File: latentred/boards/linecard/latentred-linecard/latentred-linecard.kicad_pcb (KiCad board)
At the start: 4 copper layers, 168 x 92 mm, 438 parts, among them J1 CONN_LATENTRED_LINECARD_DEVICE, J2 STEWART_SS_74500_024, Q1 SSM6N58NU, Q2 SSM6N58NU, Q3 SSM6N58NU, Q4 SSM6N58NU, Q5 SSM6N58NU, Q6 SSM6N58NU, Q7 SSM6N58NU, Q8 SSM6N58NU, U1 MCP1703T-3302E, U10 DP83867, U11 DP83867, U12 DP83867, U13 DP83867, U14 DP83867, U15 DP83867, U16 DSC6101CI2A-025.0000, U17 5PB1108CMG, U2 LTC3374-QFN, U3 SI7050, U4 LTC2451, U5 INA226, U6 INA226, U7 INA226, U8 DP83867, U9 DP83867

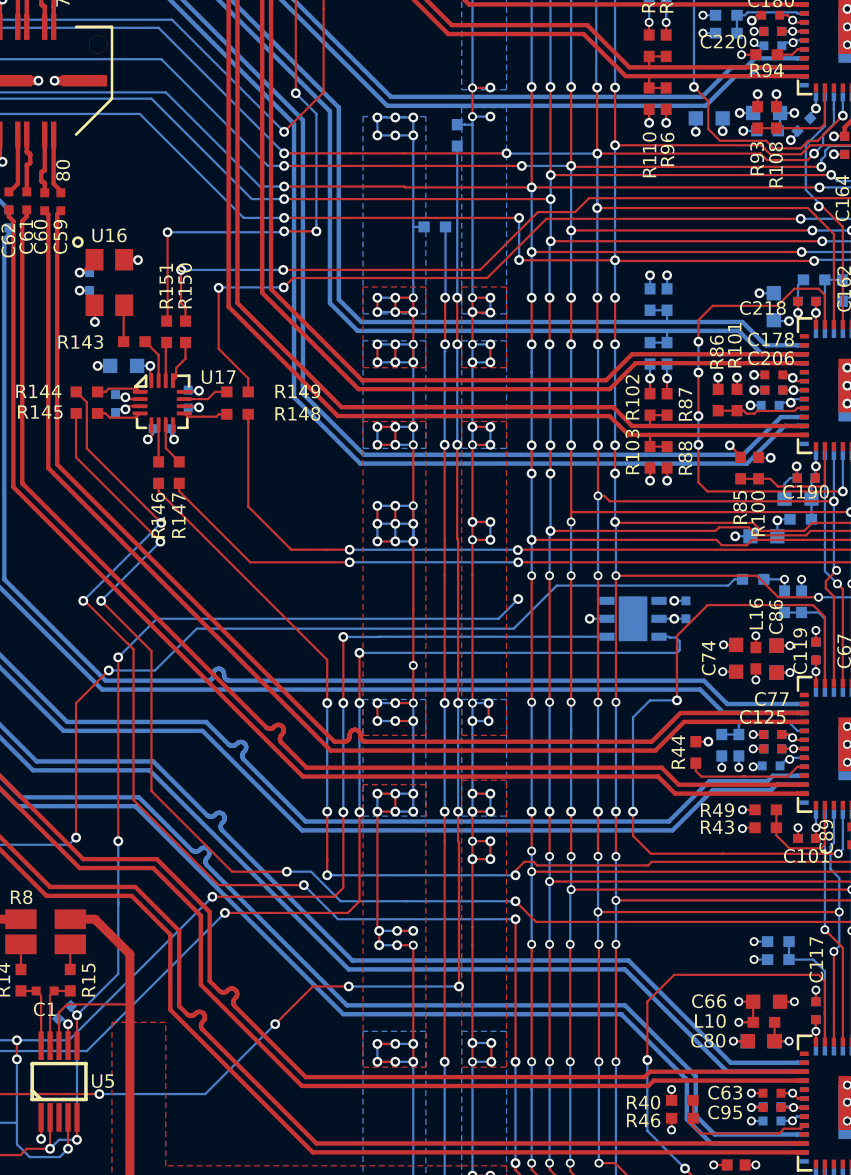
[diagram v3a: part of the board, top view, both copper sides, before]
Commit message: Continued routing line card PCB
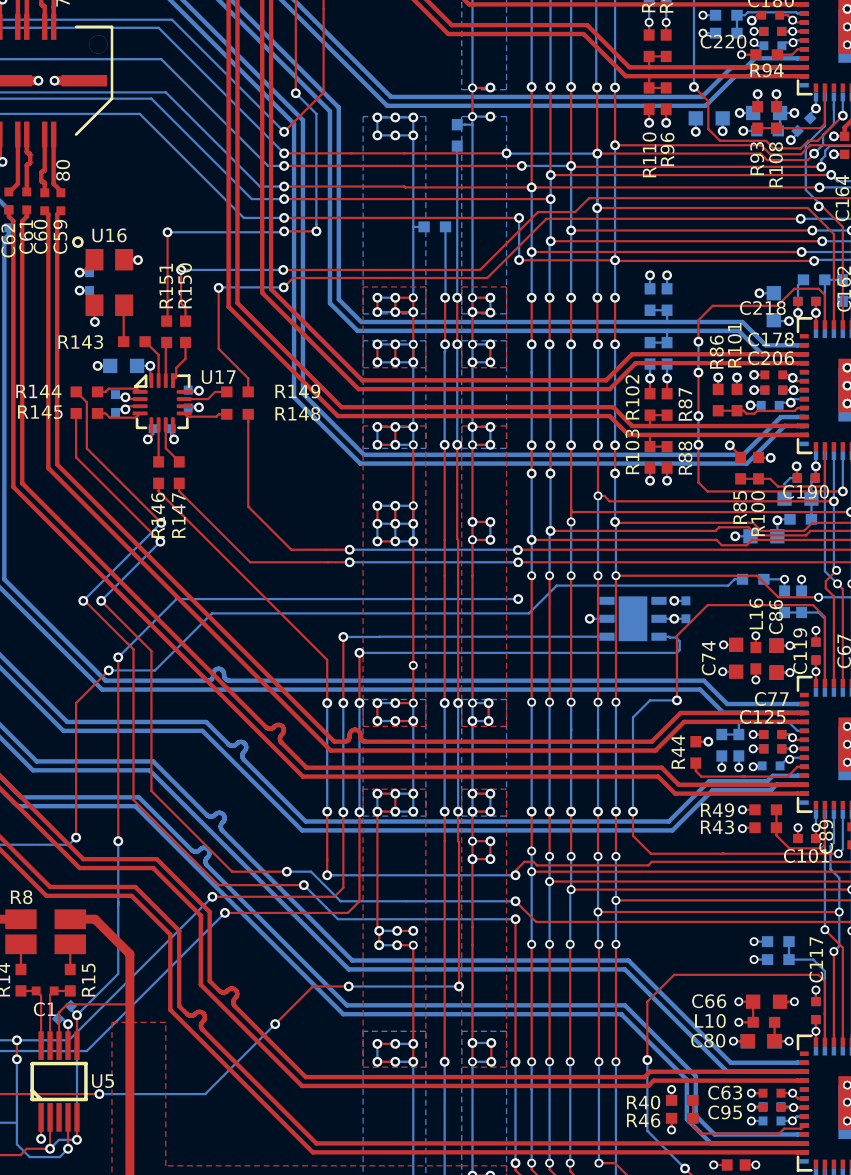
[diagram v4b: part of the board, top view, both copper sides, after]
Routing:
- net /PHYs/1V8: track 513.7 -> 516.6 mm
- net /PHYs/A2V5_1: track 14.6 -> 15.4 mm
- net /PHYs/A2V5_3: track 15.9 -> 16.5 mm
- added copper zone on In2.Cu, net /PHYs/A1V8_1
- added copper zone on In2.Cu, net /PHYs/A2V5_1
